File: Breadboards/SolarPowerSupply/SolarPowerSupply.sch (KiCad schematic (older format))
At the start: 49 parts, among them P101 CONN_01X04, P102 CONN_01X07, U101 bq25504, U102 TPS63051, U103 TPS63050

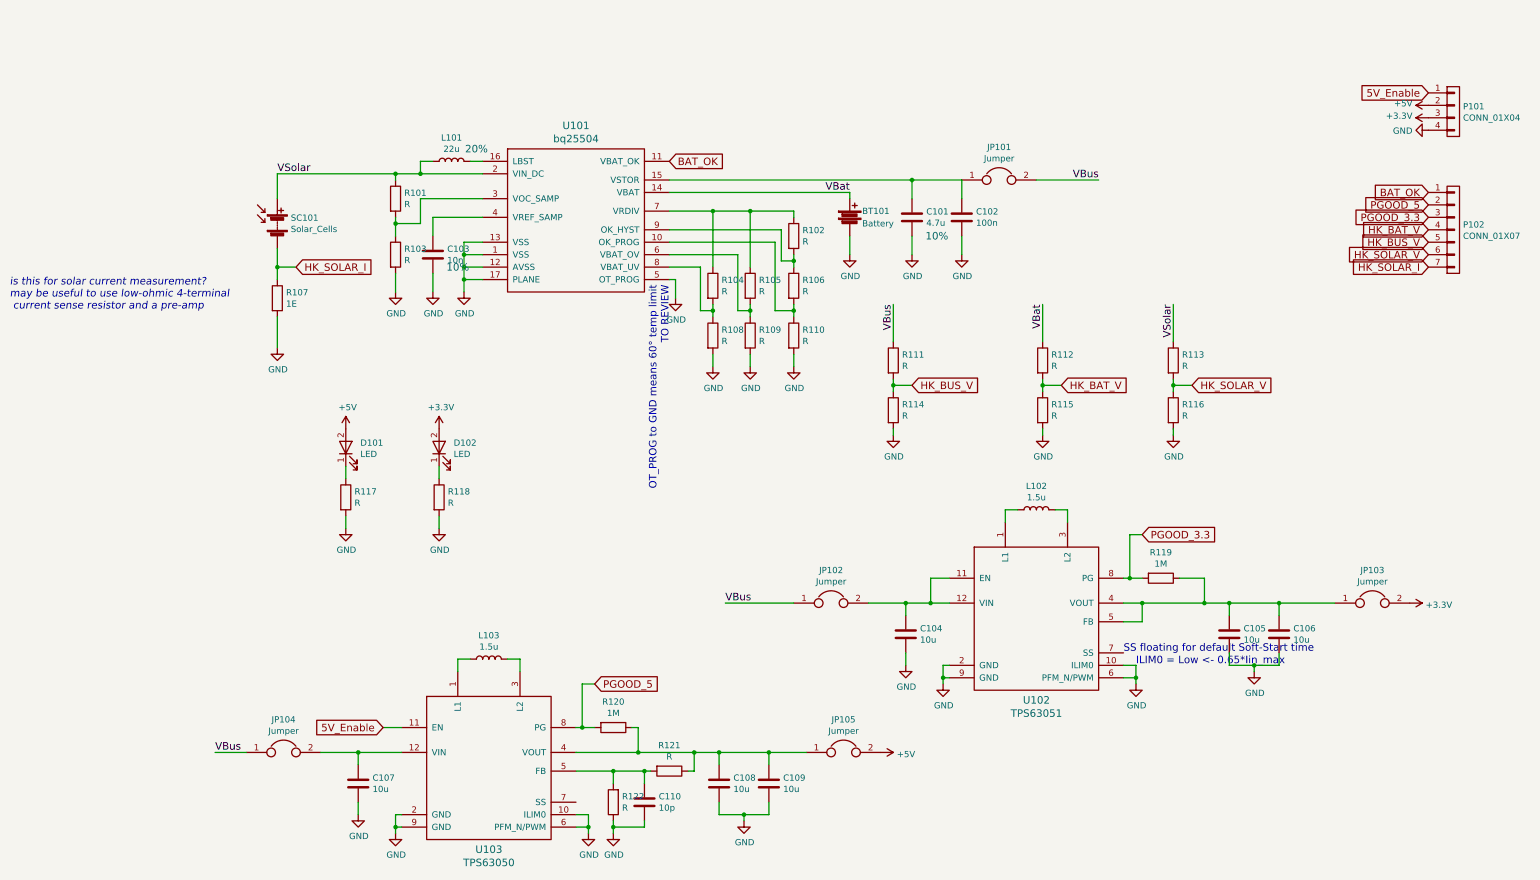
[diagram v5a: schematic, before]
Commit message: Sized all remaining resistors (except for Diodes)
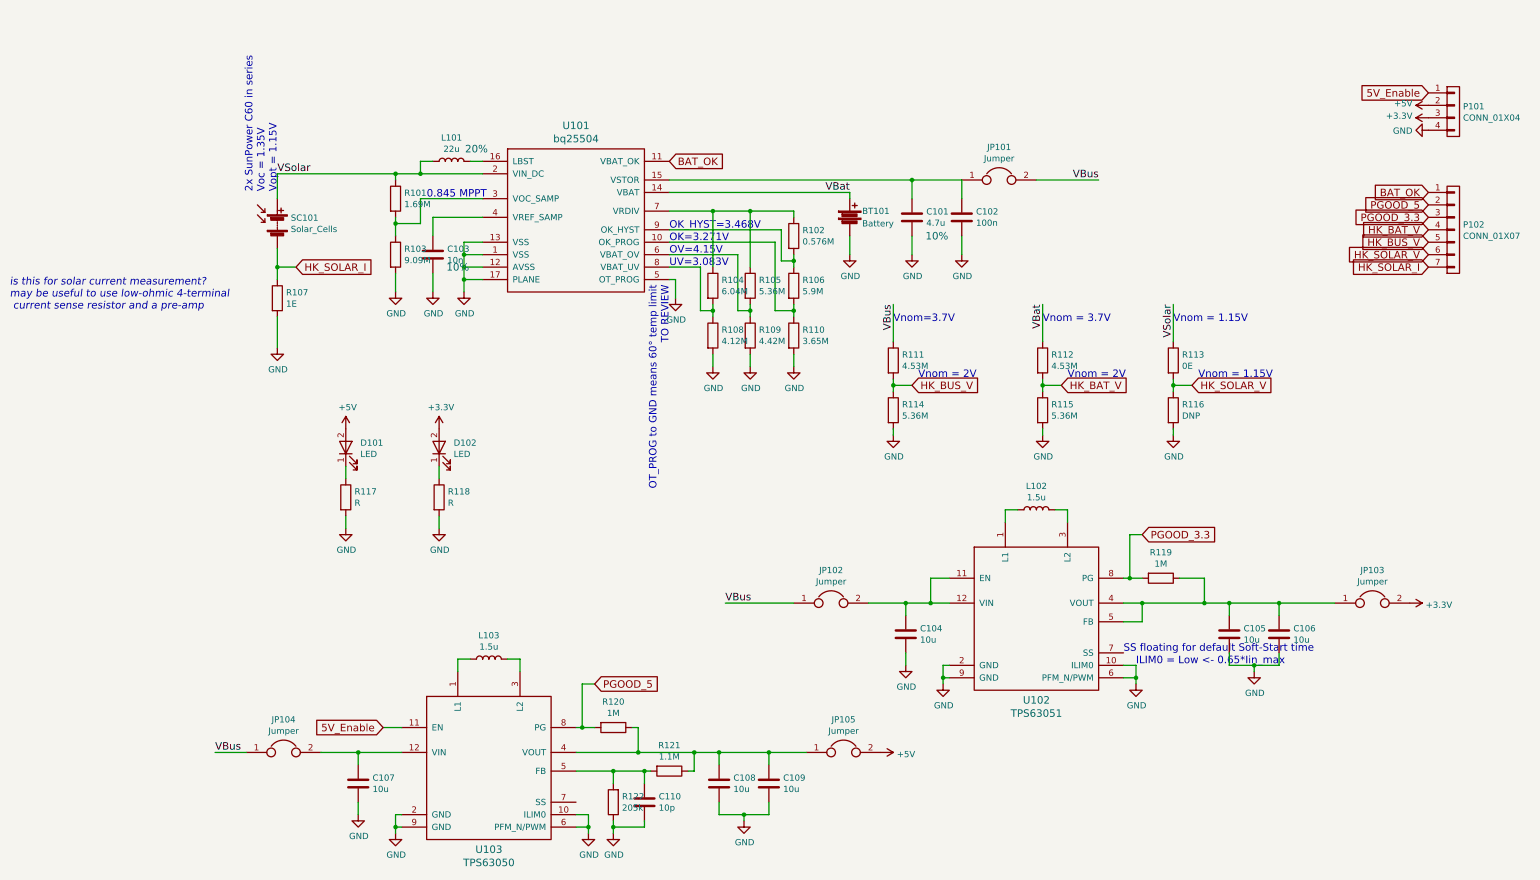
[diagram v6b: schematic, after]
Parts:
- R101: value R -> 1.69M; Tolerance (none) -> 1%
- R102: value R -> 0.576M; Tolerance (none) -> 1%
- R103: value R -> 9.09M; Tolerance (none) -> 1%
- R104: value R -> 6.04M; Tolerance (none) -> 1%
- R105, R114, R115: value R -> 5.36M; Tolerance (none) -> 1%
- R106: value R -> 5.9M; Tolerance (none) -> 1%
- R108: value R -> 4.12M; Tolerance (none) -> 1%
- R109: value R -> 4.42M; Tolerance (none) -> 1%
- R110: value R -> 3.65M; Tolerance (none) -> 1%
- R111, R112: value R -> 4.53M; Tolerance (none) -> 1%
- R113: value R -> 0E
- R116: value R -> DNP
- R121: value R -> 1.1M; Tolerance (none) -> 1%
- R122: value R -> 205k; Tolerance (none) -> 1%
- SC101: MPN (none) -> 571-282834-2; Mouser-Part 571-282834-2 -> (none)
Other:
- note added: "0.845 MPPT"
- note added: "2x SunPower C60 in series\nVoc = 1.35V\nVopt = 1.15V"
- note added: "OK=3.271V"
- note added: "OK_HYST=3.468V"
- note added: "OV=4.15V"
- note added: "UV=3.083V"
- note added: "Vnom = 1.15V"
- note added: "Vnom = 2V"
- note added: "Vnom = 3.7V"
- note added: "Vnom=3.7V"
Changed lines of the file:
@@
 P 2050 1800
 F 0 "R101" H 2120 1846 50  0000 L CNN
-F 1 "R" H 2120 1755 50  0000 L CNN
+F 1 "1.69M" H 2120 1755 50  0000 L CNN
 F 2 "Resistors_SMD:R_0603_HandSoldering" V 1980 1800 50  0001 C CNN
 F 3 "" H 2050 1800 50  0001 C CNN
+F 4 "1%" H 0   0   60  0001 C CNN "Tolerance"
 	1    2050 1800
 	1    0    0    -1
@@
 P 2050 2250
 F 0 "R103" H 2120 2296 50  0000 L CNN
-F 1 "R" H 2120 2205 50  0000 L CNN
+F 1 "9.09M" H 2120 2205 50  0000 L CNN
 F 2 "Resistors_SMD:R_0603_HandSoldering" V 1980 2250 50  0001 C CNN
 F 3 "" H 2050 2250 50  0001 C CNN
+F 4 "1%" H 0   0   60  0001 C CNN "Tolerance"
 	1    2050 2250
 	1    0    0    -1
@@
 P 5250 2100
 F 0 "R102" H 5320 2146 50  0000 L CNN
-F 1 "R" H 5320 2055 50  0000 L CNN
+F 1 "0.576M" H 5320 2055 50  0000 L CNN
 F 2 "Resistors_SMD:R_0603_HandSoldering" V 5180 2100 50  0001 C CNN
 F 3 "" H 5250 2100 50  0001 C CNN
+F 4 "1%" H 0   0   60  0001 C CNN "Tolerance"
 	1    5250 2100
 	1    0    0    -1
@@
 P 5250 2500
 F 0 "R106" H 5320 2546 50  0000 L CNN
-F 1 "R" H 5320 2455 50  0000 L CNN
+F 1 "5.9M" H 5320 2455 50  0000 L CNN
 F 2 "Resistors_SMD:R_0603_HandSoldering" V 5180 2500 50  0001 C CNN
 F 3 "" H 5250 2500 50  0001 C CNN
+F 4 "1%" H 0   0   60  0001 C CNN "Tolerance"
 	1    5250 2500
 	1    0    0    -1
@@
 P 5250 2900
 F 0 "R110" H 5320 2946 50  0000 L CNN
-F 1 "R" H 5320 2855 50  0000 L CNN
+F 1 "3.65M" H 5320 2855 50  0000 L CNN
 F 2 "Resistors_SMD:R_0603_HandSoldering" V 5180 2900 50  0001 C CNN
 F 3 "" H 5250 2900 50  0001 C CNN
+F 4 "1%" H 0   0   60  0001 C CNN "Tolerance"
 	1    5250 2900
 	1    0    0    -1
@@
 P 4900 2500
 F 0 "R105" H 4970 2546 50  0000 L CNN
-F 1 "R" H 4970 2455 50  0000 L CNN
+F 1 "5.36M" H 4970 2455 50  0000 L CNN
 F 2 "Resistors_SMD:R_0603_HandSoldering" V 4830 2500 50  0001 C CNN
 F 3 "" H 4900 2500 50  0001 C CNN
+F 4 "1%" H 0   0   60  0001 C CNN "Tolerance"
 	1    4900 2500
 	1    0    0    -1
@@
 P 4900 2900
 F 0 "R109" H 4970 2946 50  0000 L CNN
-F 1 "R" H 4970 2855 50  0000 L CNN
+F 1 "4.42M" H 4970 2855 50  0000 L CNN
 F 2 "Resistors_SMD:R_0603_HandSoldering" V 4830 2900 50  0001 C CNN
 F 3 "" H 4900 2900 50  0001 C CNN
+F 4 "1%" H 0   0   60  0001 C CNN "Tolerance"
 	1    4900 2900
 	1    0    0    -1
@@
 P 4600 2500
 F 0 "R104" H 4670 2546 50  0000 L CNN
-F 1 "R" H 4670 2455 50  0000 L CNN
+F 1 "6.04M" H 4670 2455 50  0000 L CNN
 F 2 "Resistors_SMD:R_0603_HandSoldering" V 4530 2500 50  0001 C CNN
 F 3 "" H 4600 2500 50  0001 C CNN
+F 4 "1%" H 0   0   60  0001 C CNN "Tolerance"
 	1    4600 2500
 	1    0    0    -1
@@
 P 4600 2900
 F 0 "R108" H 4670 2946 50  0000 L CNN
-F 1 "R" H 4670 2855 50  0000 L CNN
+F 1 "4.12M" H 4670 2855 50  0000 L CNN
 F 2 "Resistors_SMD:R_0603_HandSoldering" V 4530 2900 50  0001 C CNN
 F 3 "" H 4600 2900 50  0001 C CNN
+F 4 "1%" H 0   0   60  0001 C CNN "Tolerance"
 	1    4600 2900
 	1    0    0    -1
@@
 F 2 "Octanis3:TE_282834-2" V 1100 2060 50  0001 C CNN
 F 3 "" V 1100 2060 50  0001 C CNN
-F 4 "571-282834-2" H 1100 2000 60  0001 C CNN "Mouser-Part"
+F 4 "571-282834-2" H 1100 2000 60  0001 C CNN "MPN"
 	1    1100 2000
 	1    0    0    -1
@@
 P 4250 6400
 F 0 "R121" V 4043 6400 50  0000 C CNN
-F 1 "R" V 4134 6400 50  0000 C CNN
+F 1 "1.1M" V 4134 6400 50  0000 C CNN
 F 2 "Resistors_SMD:R_0603_HandSoldering" V 4180 6400 50  0001 C CNN
 F 3 "" H 4250 6400 50  0001 C CNN
+F 4 "1%" H 0   0   60  0001 C CNN "Tolerance"
 	1    4250 6400
 	0    1    1    0
@@
 P 3800 6650
 F 0 "R122" H 3730 6604 50  0000 R CNN
-F 1 "R" H 3730 6695 50  0000 R CNN
+F 1 "205k" H 3730 6695 50  0000 R CNN
 F 2 "Resistors_SMD:R_0603_HandSoldering" V 3730 6650 50  0001 C CNN
 F 3 "" H 3800 6650 50  0001 C CNN
+F 4 "1%" H 0   0   60  0001 C CNN "Tolerance"
 	1    3800 6650
 	-1   0    0    1
@@
 P 6050 3100
 F 0 "R111" H 6120 3146 50  0000 L CNN
-F 1 "R" H 6120 3055 50  0000 L CNN
+F 1 "4.53M" H 6120 3055 50  0000 L CNN
 F 2 "Resistors_SMD:R_0603_HandSoldering" V 5980 3100 50  0001 C CNN
 F 3 "" H 6050 3100 50  0001 C CNN
+F 4 "1%" H 0   0   60  0001 C CNN "Tolerance"
 	1    6050 3100
 	1    0    0    -1
@@
 P 6050 3500
 F 0 "R114" H 6120 3546 50  0000 L CNN
-F 1 "R" H 6120 3455 50  0000 L CNN
+F 1 "5.36M" H 6120 3455 50  0000 L CNN
 F 2 "Resistors_SMD:R_0603_HandSoldering" V 5980 3500 50  0001 C CNN
 F 3 "" H 6050 3500 50  0001 C CNN
+F 4 "1%" H 0   0   60  0001 C CNN "Tolerance"
 	1    6050 3500
 	1    0    0    -1
@@
 P 7250 3100
 F 0 "R112" H 7320 3146 50  0000 L CNN
-F 1 "R" H 7320 3055 50  0000 L CNN
+F 1 "4.53M" H 7320 3055 50  0000 L CNN
 F 2 "Resistors_SMD:R_0603_HandSoldering" V 7180 3100 50  0001 C CNN
 F 3 "" H 7250 3100 50  0001 C CNN
+F 4 "1%" H 0   0   60  0001 C CNN "Tolerance"
 	1    7250 3100
 	1    0    0    -1
@@
 P 7250 3500
 F 0 "R115" H 7320 3546 50  0000 L CNN
-F 1 "R" H 7320 3455 50  0000 L CNN
+F 1 "5.36M" H 7320 3455 50  0000 L CNN
 F 2 "Resistors_SMD:R_0603_HandSoldering" V 7180 3500 50  0001 C CNN
 F 3 "" H 7250 3500 50  0001 C CNN
+F 4 "1%" H 0   0   60  0001 C CNN "Tolerance"
 	1    7250 3500
 	1    0    0    -1
@@
 P 8300 3100
 F 0 "R113" H 8370 3146 50  0000 L CNN
-F 1 "R" H 8370 3055 50  0000 L CNN
+F 1 "0E" H 8370 3055 50  0000 L CNN
 F 2 "Resistors_SMD:R_0603_HandSoldering" V 8230 3100 50  0001 C CNN
 F 3 "" H 8300 3100 50  0001 C CNN
@@
 P 8300 3500
 F 0 "R116" H 8370 3546 50  0000 L CNN
-F 1 "R" H 8370 3455 50  0000 L CNN
+F 1 "DNP" H 8370 3455 50  0000 L CNN
 F 2 "Resistors_SMD:R_0603_HandSoldering" V 8230 3500 50  0001 C CNN
 F 3 "" H 8300 3500 50  0001 C CNN
@@
 Text GLabel 10350 950  0    60   Input ~ 0
 5V_Enable
+Text Notes 2300 1800 0    60   ~ 0
+0.845 MPPT
+Text Notes 4250 2250 0    60   ~ 0
+OV=4.15V
+Text Notes 4250 2350 0    60   ~ 0
+UV=3.083V
+Text Notes 4250 2050 0    60   ~ 0
+OK_HYST=3.468V
+Text Notes 4250 2150 0    60   ~ 0
+OK=3.271V
+Text Notes 1100 1750 1    60   ~ 0
+2x SunPower C60 in series\nVoc = 1.35V\nVopt = 1.15V
+Text Notes 8300 2800 0    60   ~ 0
+Vnom = 1.15V
+Text Notes 8500 3250 0    60   ~ 0
+Vnom = 1.15V
+Text Notes 7250 2800 0    60   ~ 0
+Vnom = 3.7V
+Text Notes 6050 2800 0    60   ~ 0
+Vnom=3.7V
+Text Notes 7450 3250 0    60   ~ 0
+Vnom = 2V
+Text Notes 6250 3250 0    60   ~ 0
+Vnom = 2V
 $EndSCHEMATC

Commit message: Adds MPN for most resistances.
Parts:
- R101: MPN (none) -> 71-CRCW06031M69FKEA
- R102: MPN (none) -> 71-CRCW0603-576K-E3
- R103: MPN (none) -> 71-CRCW06039M09FKEA
- R104: MPN (none) -> 71-CRCW06036M04FKEA
- R105, R114, R115: MPN (none) -> 71-CRCW06035M36FKEA
- R106: MPN (none) -> 71-CRCW06035M90FKEA
- R108: MPN (none) -> 71-CRCW06034M12FKEA
- R109: MPN (none) -> 71-CRCW06034M42FKEA
- R110: MPN (none) -> 71-CRCW0603-3.65M-E3
- R111, R112: MPN (none) -> 71-CRCW06034M53FKEA
- R121: MPN (none) -> 71-CRCW06031M10JNEA
- R122: MPN (none) -> 71-CRCW0603-205K-E3
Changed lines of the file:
@@
 F 3 "" H 2050 1800 50  0001 C CNN
 F 4 "1%" H 0   0   60  0001 C CNN "Tolerance"
+F 5 "71-CRCW06031M69FKEA" H 2050 1800 60  0001 C CNN "MPN"
 	1    2050 1800
 	1    0    0    -1
@@
 F 3 "" H 2050 2250 50  0001 C CNN
 F 4 "1%" H 0   0   60  0001 C CNN "Tolerance"
+F 5 "71-CRCW06039M09FKEA" H 0   0   60  0001 C CNN "MPN"
 	1    2050 2250
 	1    0    0    -1
@@
 F 3 "" H 5250 2100 50  0001 C CNN
 F 4 "1%" H 0   0   60  0001 C CNN "Tolerance"
+F 5 "71-CRCW0603-576K-E3" H 0   0   60  0001 C CNN "MPN"
 	1    5250 2100
 	1    0    0    -1
@@
 F 3 "" H 5250 2500 50  0001 C CNN
 F 4 "1%" H 0   0   60  0001 C CNN "Tolerance"
+F 5 "71-CRCW06035M90FKEA" H 0   0   60  0001 C CNN "MPN"
 	1    5250 2500
 	1    0    0    -1
@@
 F 3 "" H 5250 2900 50  0001 C CNN
 F 4 "1%" H 0   0   60  0001 C CNN "Tolerance"
+F 5 "71-CRCW0603-3.65M-E3" H 0   0   60  0001 C CNN "MPN"
 	1    5250 2900
 	1    0    0    -1
@@
 F 3 "" H 4900 2500 50  0001 C CNN
 F 4 "1%" H 0   0   60  0001 C CNN "Tolerance"
+F 5 "71-CRCW06035M36FKEA" H 0   0   60  0001 C CNN "MPN"
 	1    4900 2500
 	1    0    0    -1
@@
 F 3 "" H 4900 2900 50  0001 C CNN
 F 4 "1%" H 0   0   60  0001 C CNN "Tolerance"
+F 5 "71-CRCW06034M42FKEA" H 0   0   60  0001 C CNN "MPN"
 	1    4900 2900
 	1    0    0    -1
@@
 F 3 "" H 4600 2500 50  0001 C CNN
 F 4 "1%" H 0   0   60  0001 C CNN "Tolerance"
+F 5 "71-CRCW06036M04FKEA" H 0   0   60  0001 C CNN "MPN"
 	1    4600 2500
 	1    0    0    -1
@@
 F 3 "" H 4600 2900 50  0001 C CNN
 F 4 "1%" H 0   0   60  0001 C CNN "Tolerance"
+F 5 "71-CRCW06034M12FKEA" H 0   0   60  0001 C CNN "MPN"
 	1    4600 2900
 	1    0    0    -1
@@
 F 3 "" H 4250 6400 50  0001 C CNN
 F 4 "1%" H 0   0   60  0001 C CNN "Tolerance"
+F 5 "71-CRCW06031M10JNEA" H 0   0   60  0001 C CNN "MPN"
 	1    4250 6400
 	0    1    1    0
@@
 F 3 "" H 3800 6650 50  0001 C CNN
 F 4 "1%" H 0   0   60  0001 C CNN "Tolerance"
+F 5 "71-CRCW0603-205K-E3" H 0   0   60  0001 C CNN "MPN"
 	1    3800 6650
 	-1   0    0    1
@@
 F 3 "" H 6050 3100 50  0001 C CNN
 F 4 "1%" H 0   0   60  0001 C CNN "Tolerance"
+F 5 "71-CRCW06034M53FKEA" H 0   0   60  0001 C CNN "MPN"
 	1    6050 3100
 	1    0    0    -1
@@
 F 3 "" H 6050 3500 50  0001 C CNN
 F 4 "1%" H 0   0   60  0001 C CNN "Tolerance"
+F 5 "71-CRCW06035M36FKEA" H 0   0   60  0001 C CNN "MPN"
 	1    6050 3500
 	1    0    0    -1
@@
 F 3 "" H 7250 3100 50  0001 C CNN
 F 4 "1%" H 0   0   60  0001 C CNN "Tolerance"
+F 5 "71-CRCW06034M53FKEA" H 0   0   60  0001 C CNN "MPN"
 	1    7250 3100
 	1    0    0    -1
@@
 F 3 "" H 7250 3500 50  0001 C CNN
 F 4 "1%" H 0   0   60  0001 C CNN "Tolerance"
+F 5 "71-CRCW06035M36FKEA" H 0   0   60  0001 C CNN "MPN"
 	1    7250 3500
 	1    0    0    -1

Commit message: Added MPN for missing parts
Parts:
- R107: MPN (none) -> 603-RC1206DR-071RL
- R119, R120: MPN (none) -> 71-CRCW06031M10JNEA
- U101: MPN (none) -> 595-BQ25504RGTT
- U102: MPN (none) -> 595-TPS63051RMWT
- U103: MPN (none) -> 595-TPS63050RMWR
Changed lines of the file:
@@
 F 2 "Housings_DFN_QFN:QFN-16-1EP_3x3mm_Pitch0.5mm" H 2950 1400 60  0001 C CNN
 F 3 "" H 2950 1400 60  0001 C CNN
+F 4 "595-BQ25504RGTT" H 0   0   60  0001 C CNN "MPN"
 	1    2950 1400
 	1    0    0    -1
@@
 F 2 "Octanis3:VQFN_12_2.5x2.5mm" H 6700 4600 60  0001 C CNN
 F 3 "" H 6700 4600 60  0001 C CNN
+F 4 "595-TPS63051RMWT" H 0   0   60  0001 C CNN "MPN"
 	1    6700 4600
 	1    0    0    -1
@@
 F 2 "Resistors_SMD:R_0603_HandSoldering" V 8130 4850 50  0001 C CNN
 F 3 "" H 8200 4850 50  0001 C CNN
+F 4 "71-CRCW06031M10JNEA" H 0   0   60  0001 C CNN "MPN"
 	1    8200 4850
 	0    1    1    0
@@
 F 2 "Resistors_SMD:R_0603_HandSoldering" V 3730 6050 50  0001 C CNN
 F 3 "" H 3800 6050 50  0001 C CNN
+F 4 "71-CRCW06031M10JNEA" H 0   0   60  0001 C CNN "MPN"
 	1    3800 6050
 	0    1    1    0
@@
 F 2 "Octanis3:VQFN_12_2.5x2.5mm" H 2300 5800 60  0001 C CNN
 F 3 "" H 2300 5800 60  0001 C CNN
+F 4 "595-TPS63050RMWR" H 0   0   60  0001 C CNN "MPN"
 	1    2300 5800
 	1    0    0    -1
@@
 F 2 "Resistors_SMD:R_1206_HandSoldering" V 1030 2600 50  0001 C CNN
 F 3 "" H 1100 2600 50  0001 C CNN
+F 4 "603-RC1206DR-071RL" H 0   0   60  0001 C CNN "MPN"
 	1    1100 2600
 	1    0    0    -1
